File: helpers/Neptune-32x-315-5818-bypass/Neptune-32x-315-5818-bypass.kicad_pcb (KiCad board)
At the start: 2 copper layers, 24.4 x 24.4 mm, 1 part, among them IC1 315-5818

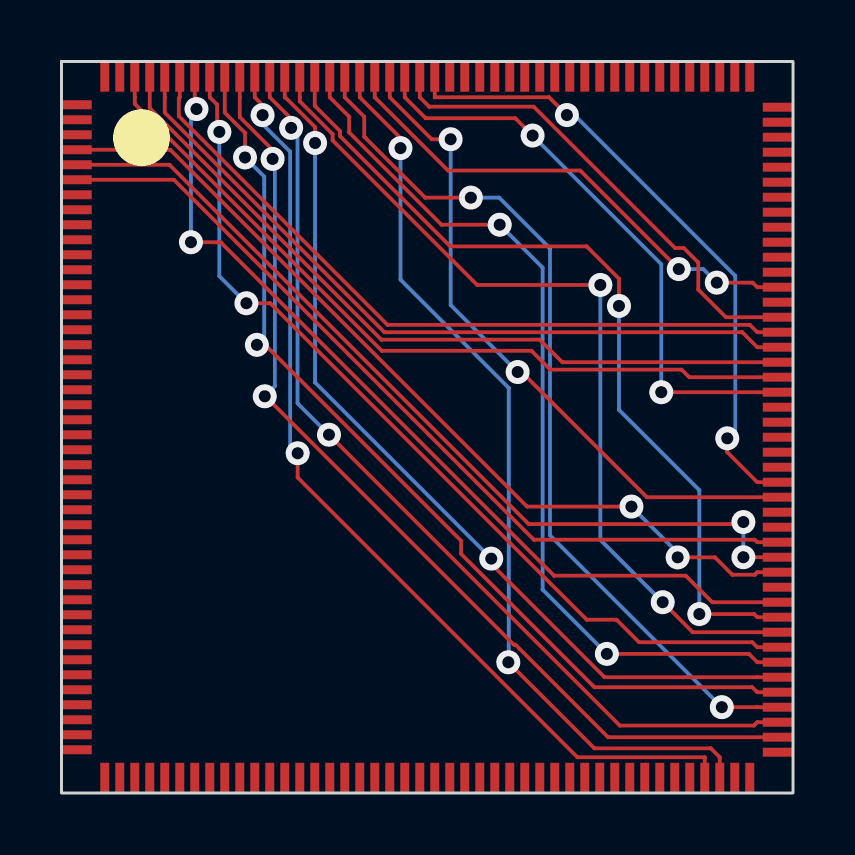
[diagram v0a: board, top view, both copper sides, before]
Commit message: Update bypass flexes for 315-5805 and 315-5818 for better connection (issue #11).
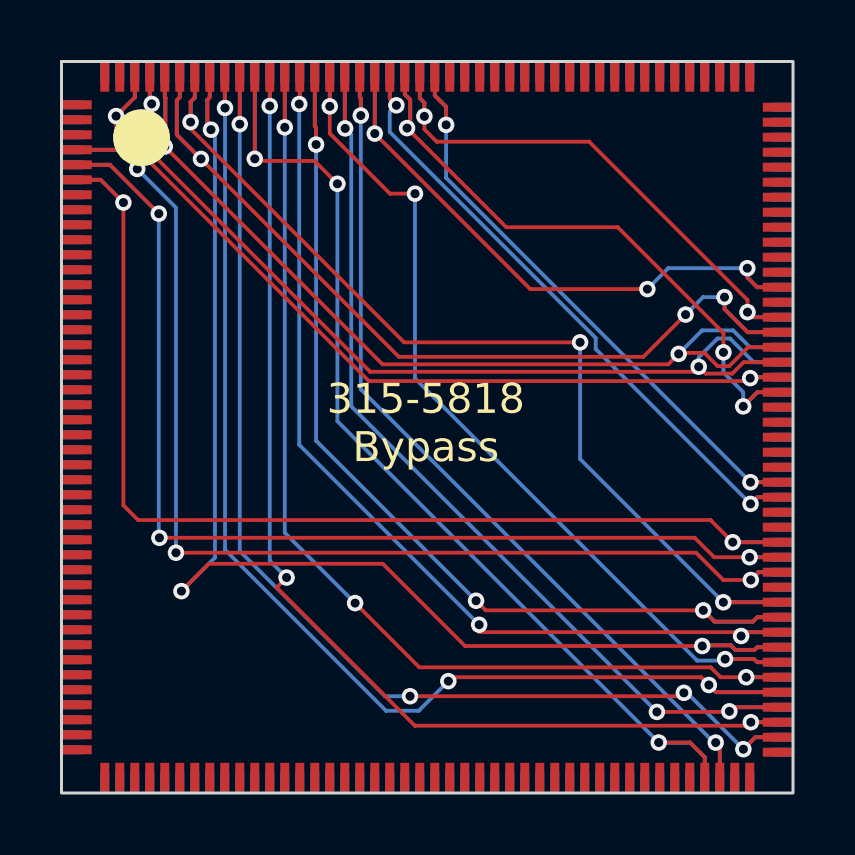
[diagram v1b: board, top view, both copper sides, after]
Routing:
- net VD10: track 30.5 -> 43.7 mm, vias 2 -> 3
- net VA19: track 29.4 -> 39.4 mm, vias 2 -> 3
- net VA20: track 29.5 -> 39.5 mm, vias 2 -> 3
- net VA21: track 28.4 -> 37.7 mm, vias 0 -> 2
- net VD9: track 32.0 -> 40.4 mm, vias 2 -> 3
- net VD12: track 24.3 -> 32.2 mm, vias 0 -> 3
- net VD13: track 24.9 -> 32.6 mm, vias 0 -> 2
- net VD8: track 33.1 -> 39.6 mm, vias 2 -> 4
- net VD3: track 28.5 -> 35.1 mm, vias 2 -> 3
- net VD6: track 31.8 -> 37.9 mm, vias 2 -> 3
- net VD5: track 30.2 -> 36.4 mm, vias 2 -> 3
- net VD14: track 25.5 -> 31.3 mm, vias 0 -> 2
- net ~{CLWR}: track 16.7 -> 21.6 mm, vias 2 -> 3
- net VD7: track 32.1 -> 36.5 mm, vias 2 -> 3
- net VD4: track 29.2 -> 33.5 mm, vias 2 -> 3
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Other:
- board text added: "315-5818 Bypass"
